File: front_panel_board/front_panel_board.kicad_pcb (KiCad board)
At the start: 2 copper layers, 70 x 35 mm, 15 parts, among them J1 Molex_SL_01x02_Male, J2 Conn_02x05_Odd_Even, J3 Conn_02x05_Odd_Even, J4 Molex_SL_01x02_Male, SW1 SW_Rotary8_CK_A125xxxxCxx, SW2 SW_SPST

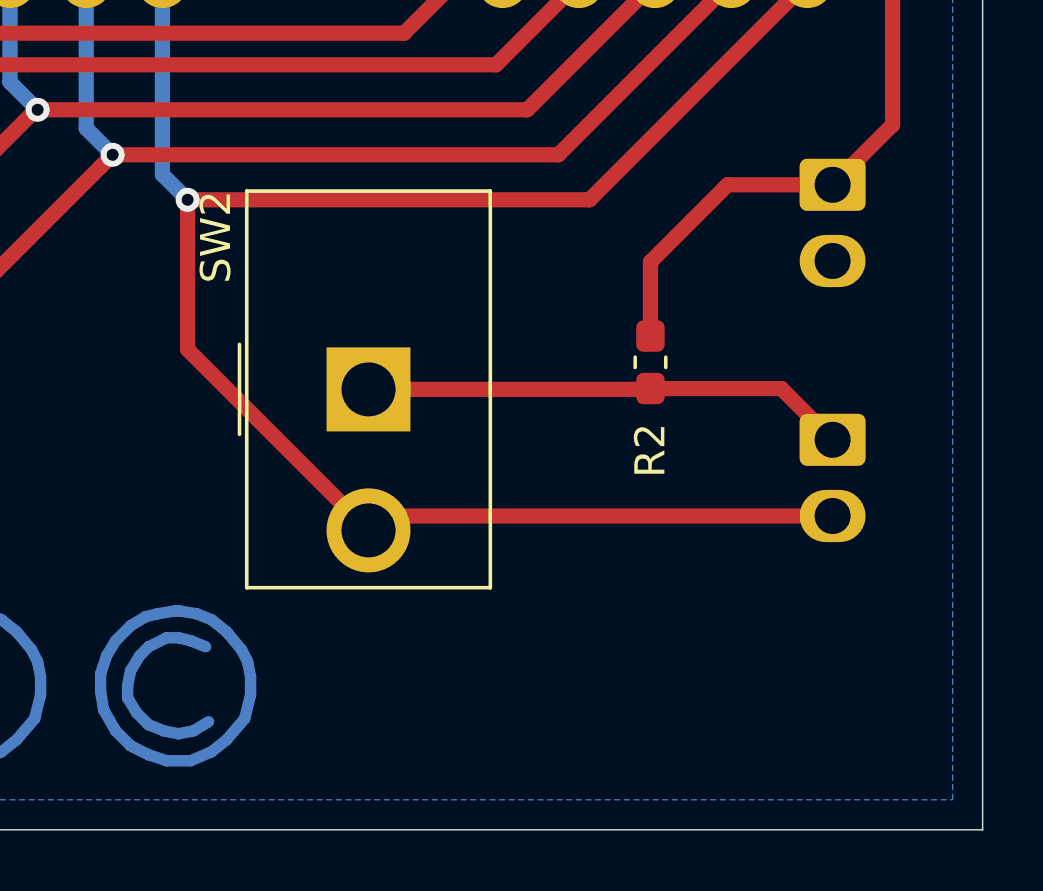
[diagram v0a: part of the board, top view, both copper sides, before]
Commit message: update net labelling, change to SPDT switch for headphone selection, and clean up schematic
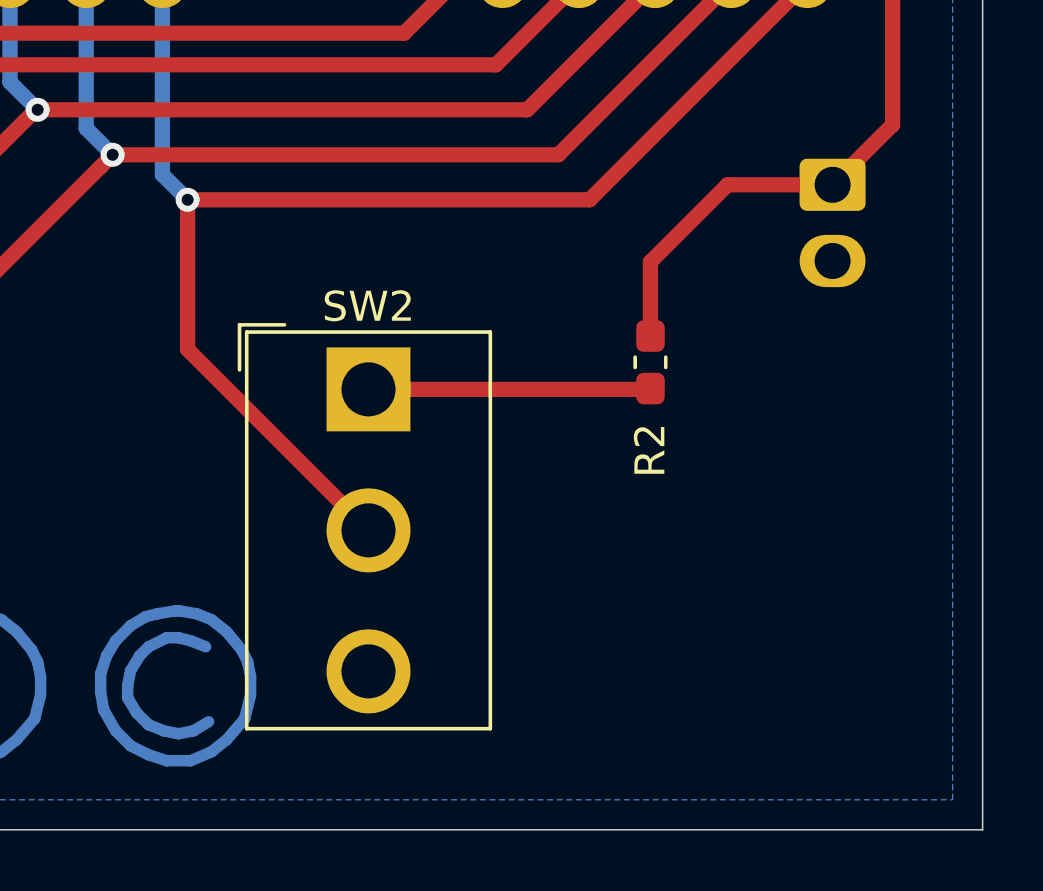
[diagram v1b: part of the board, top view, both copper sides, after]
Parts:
- removed J4: Molex_SL_01x02_Male, Connector_Molex_SL:Molex_SL_A-70543-0001_1x02_P2.54mm_Vertical
- SW2: value SW_SPST -> SW_SPDT; footprint Button_Switch_THT_gkeeth:SW_Toggle_SPST_NKK_M2011xxx03 -> Button_Switch_THT_gkeeth:SW_Toggle_SPDT_NKK_M201xxxx03
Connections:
- net /output_mute_select renamed /headphone_select
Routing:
- net /headphone_select: track 60.9 -> 45.2 mm
- net Net-(R2-Pad2): track 16.2 -> 9.41 mm
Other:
- board text added: "TODO Move headphone switch in line with input switch decide on orientation for headphone switch (which way should be up?) Place power LED headers on back fit in enclosure packaging?"

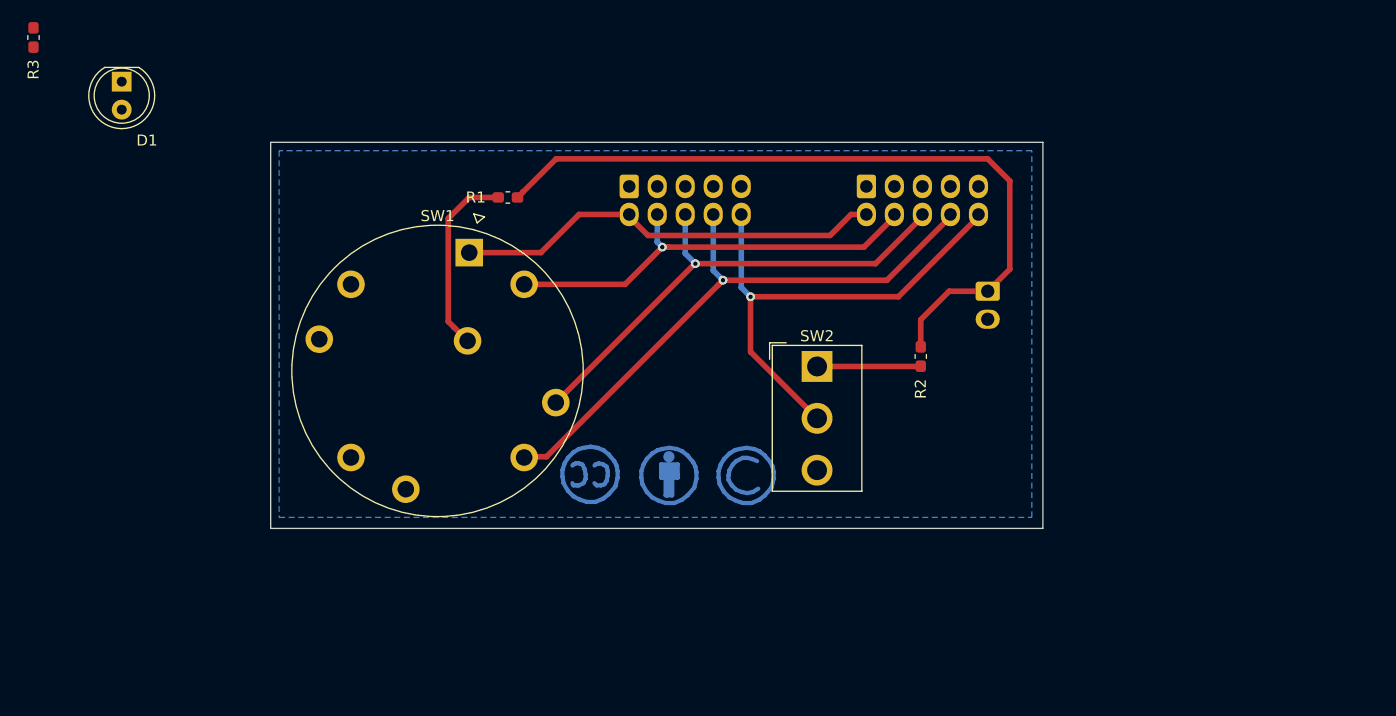
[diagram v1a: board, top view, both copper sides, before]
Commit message: change relay resistors to 0805 and label headphone switch
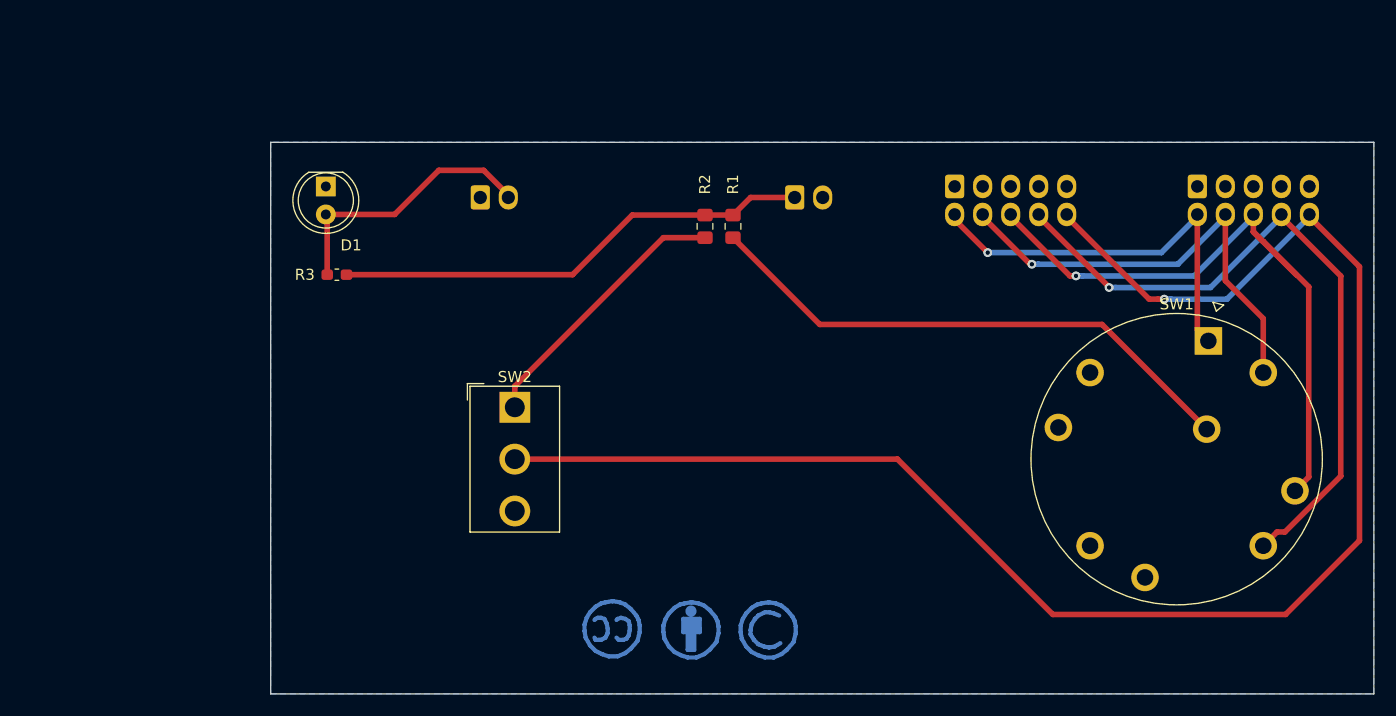
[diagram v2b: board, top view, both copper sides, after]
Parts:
- added J4: Molex_SL_01x02_Male, Connector_Molex_SL:Molex_SL_A-70543-0001_1x02_P2.54mm_Vertical, B.Cu at (120.6, 55.8)
- R1, R2: footprint Resistor_SMD:R_0603_1608Metric_Pad1.05x0.95mm_HandSolder -> Resistor_SMD:R_0805_2012Metric_Pad1.15x1.40mm_HandSolder
- moved SW1 67.5 mm to (186.6, 68.8)
- moved REF** 40.1 mm to (124.1, 94.8)
- moved REF** 40.1 mm to (112.6, 94.8)
- moved R3 34.9 mm to (107.6, 62.8), turned to 180 degrees
- moved J2 30.0 mm to (185.6, 54.8)
- moved J3 29.5 mm to (163.6, 54.8)
- moved SW2 27.6 mm to (123.7, 74.8)
- moved R2 22.8 mm to (141.0, 58.4)
- moved D1 20.8 mm to (106.6, 54.8)
- moved R1 20.6 mm to (143.5, 58.4), turned to 270 degrees
- moved J1 19.5 mm to (149.1, 55.8), turned to 0 degrees
- moved REF** 14.1 mm to (146.7, 95.0)
- moved REF** 14.1 mm to (139.7, 95.0)
- moved REF** 14.1 mm to (132.7, 95.0)
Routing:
- net /headphone_select: track 45.2 -> 145.2 mm
- net Net-(R1-Pad2): track 17.1 -> 50.1 mm
- net Net-(D1-Pad2): track 0.00 -> 24.9 mm
- net Vrelay: track 67.3 -> 43.5 mm
- net Net-(R2-Pad2): track 9.41 -> 24.7 mm
- net /input3_select: track 45.3 -> 60.1 mm
- net /input4_select: track 54.2 -> 63.3 mm
- net /input2_select: track 39.5 -> 41.7 mm
- net /input1_select: track 39.1 -> 37.1 mm, vias 0 -> 1
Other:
- board size 70 x 35 mm -> 100 x 50 mm
- board text added: "Front Panel Board rev0 Preamp 2019 G. Keeth 2019-09-28"
- board text added: "TODO Place power LED"
- board text removed: "Front Panel Board rev0 Preamp 2019 G. Keeth 2019-06-09"
- board text removed: "TODO Move headphone switch in line with input switch decide on orientation for headphone switch (which way should be up?) Place power LED headers on back fit in enclosure packaging?"
